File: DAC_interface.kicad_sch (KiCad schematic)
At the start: 2 parts

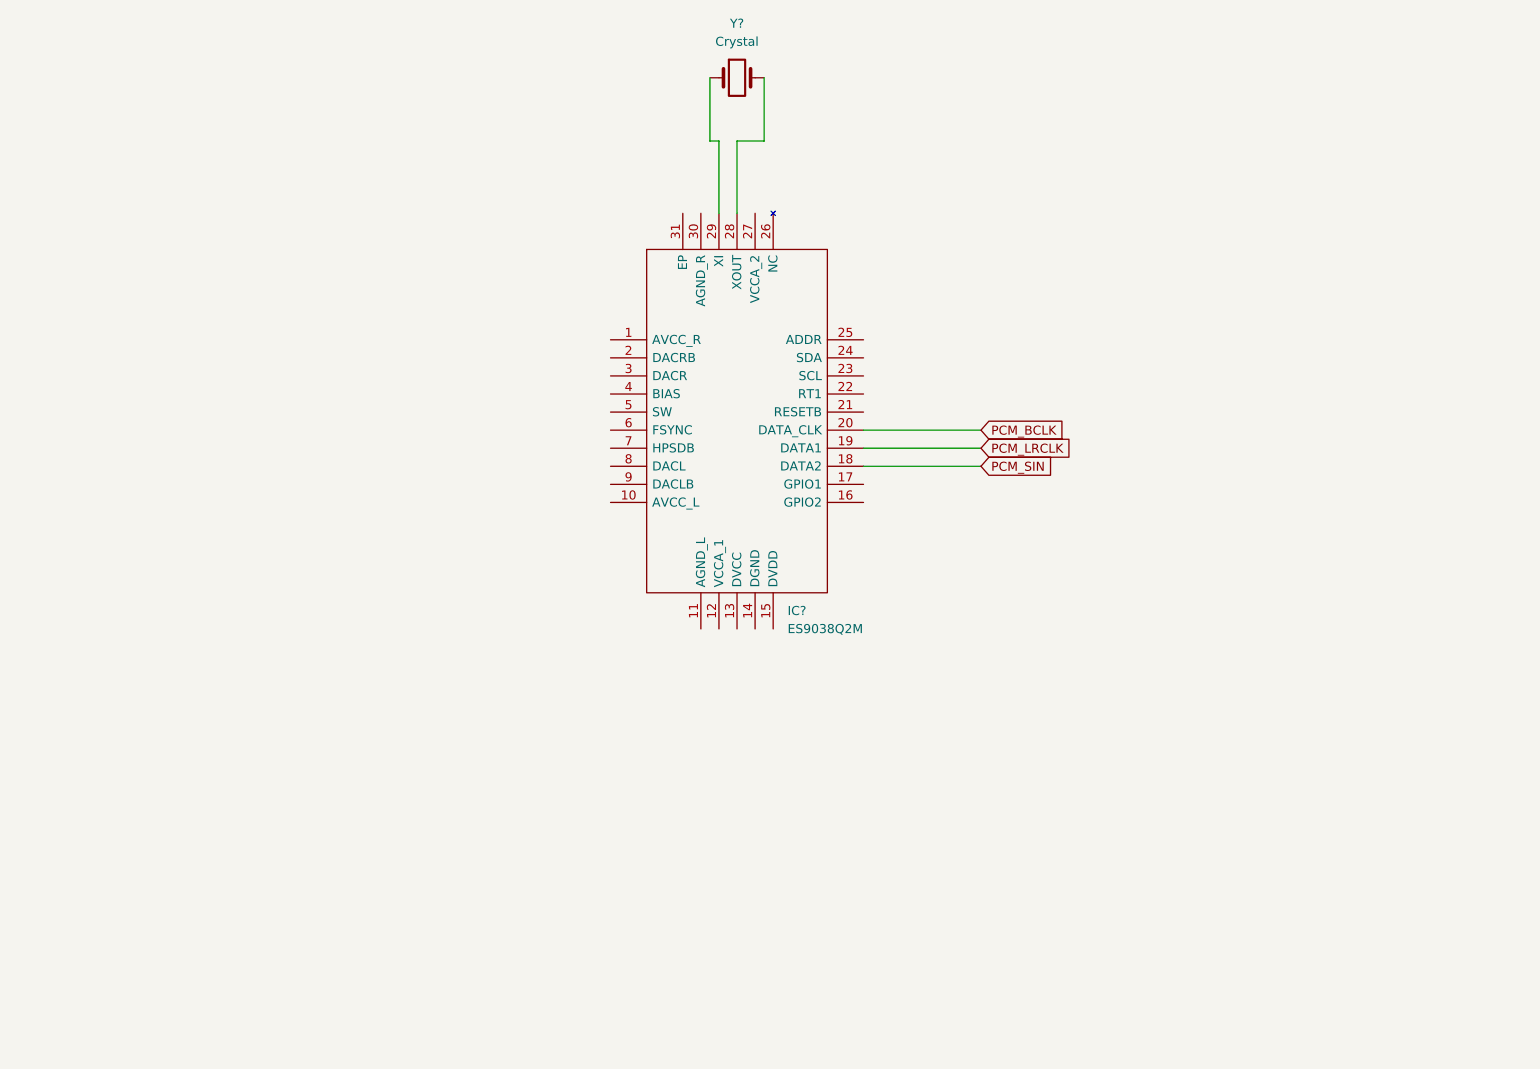
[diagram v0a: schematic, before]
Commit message: Adding ES9038q2m configuration
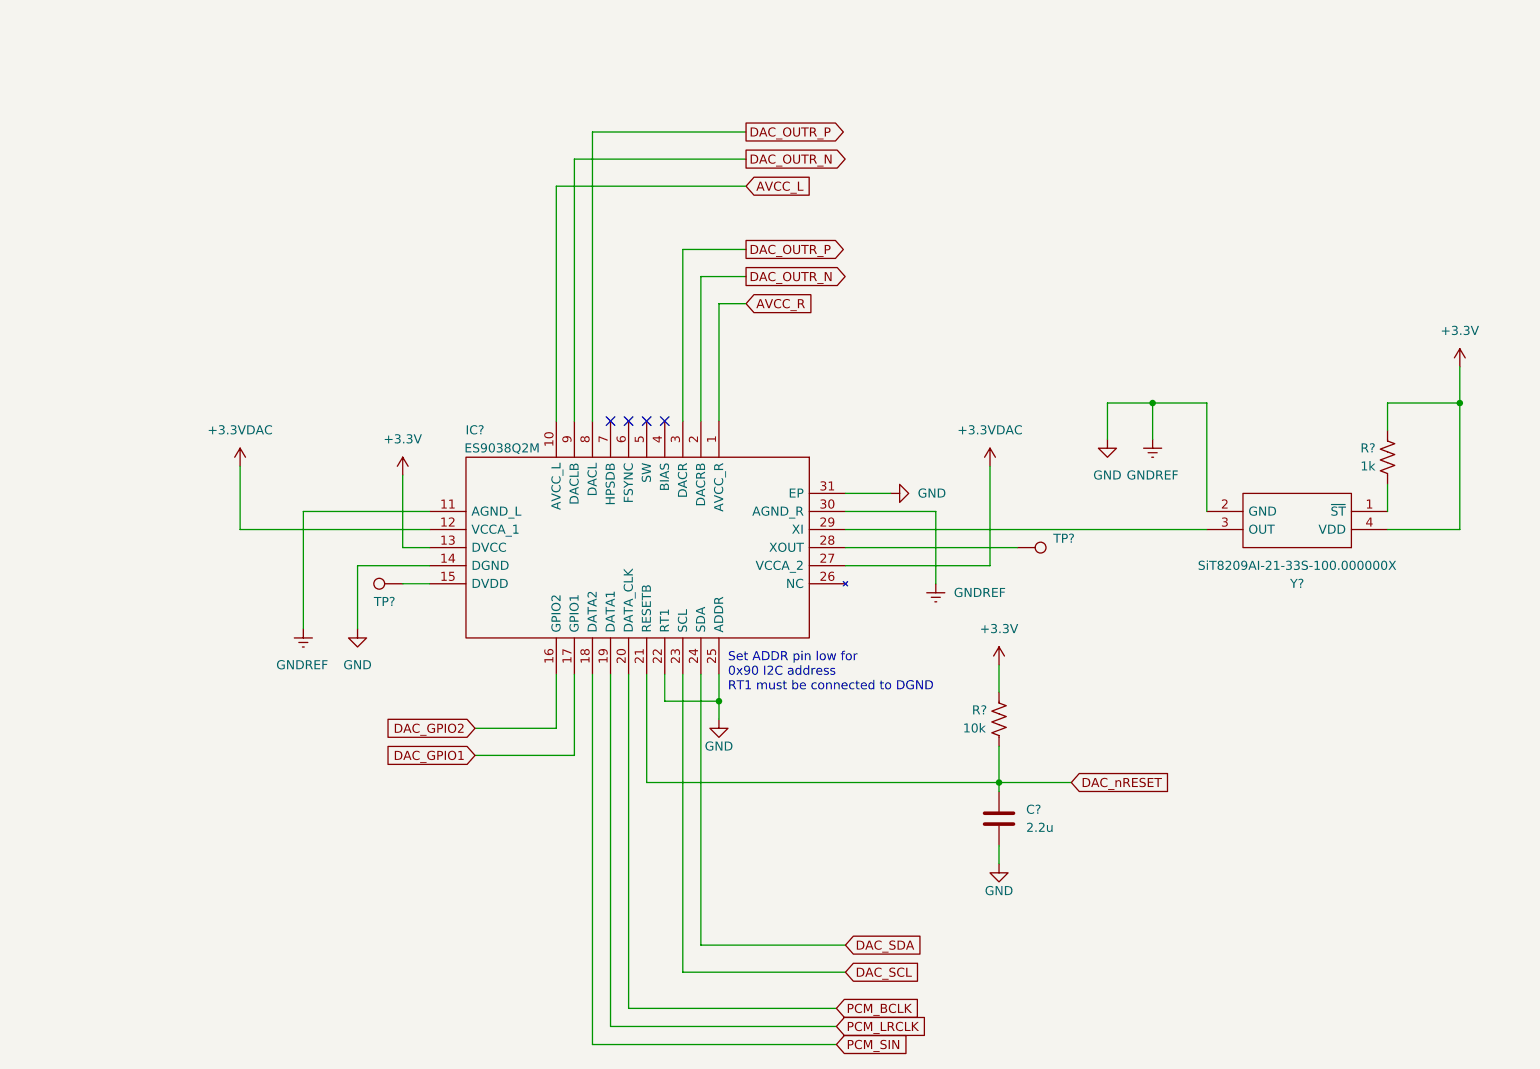
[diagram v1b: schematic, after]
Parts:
- removed Y?: Crystal, symbol Device:Crystal
- added C?: 2.2u, symbol Device:C
- added R?: 10k, symbol Device:R_US
- added R?: 1k, symbol Device:R_US
- added TP? (x2): TestPoint, symbol Connector:TestPoint
- added Y?: SiT8209AI-21-33S-100.000000X, SiT8209AI2133S100000000X, symbol SamacSys_Parts:SiT8209AI-21-33S-100.000000X
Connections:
- net at IC?.29 (XI): now also Y?.3 (OUT)
- net at IC?.28 (XOUT): now also TP?.1
- net AVCC_R: now reaches IC?.1 (AVCC_R)
- net AVCC_L: now reaches IC?.10 (AVCC_L)
- net GND: now reaches IC?.11 (AGND_L)
- net GND: now also IC?.14 (DGND), IC?.22 (RT1), IC?.25 (ADDR), IC?.30 (AGND_R), IC?.31 (EP), C?.2, Y?.2 (GND)
- net +3.3VDAC: now reaches IC?.12 (VCCA_1)
- net +3.3VDAC: now also IC?.27 (VCCA_2)
- net +3V3: now reaches IC?.13 (DVCC)
- net +3V3: now also R?.1, R?.1, Y?.4 (VDD)
- net at IC?.15 (DVDD): now also TP?.1
- net DAC_GPIO2: now reaches IC?.16 (GPIO2)
- net DAC_GPIO1: now reaches IC?.17 (GPIO1)
- net DAC_OUTR_N: now reaches IC?.2 (DACRB)
- net DAC_OUTR_N: now also IC?.9 (DACLB)
- net DAC_nRESET: now reaches IC?.21 (RESETB)
- net DAC_nRESET: now also C?.1, R?.2
- net DAC_SCL: now reaches IC?.23 (SCL)
- net DAC_SDA: now reaches IC?.24 (SDA)
- net DAC_OUTR_P: now reaches IC?.3 (DACR)
- net DAC_OUTR_P: now also IC?.8 (DACL)
- new net: R?.2, Y?.1 (~{ST})
- no-connect marks 0 -> 4
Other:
- note added: "Set ADDR pin low for 0x90 I2C address RT1 must be connected to DGND"
- title: (none) -> ES9038Q2M DAC Interface
- moved on the sheet: IC?

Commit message: WIP output stage
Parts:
- removed TP?: TestPoint, symbol Connector:TestPoint
- added C? (x2): 2.2u, symbol Device:C
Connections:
- net GND: now also C?.2, C?.2
- net at IC?.15 (DVDD): now also C?.1, C?.1
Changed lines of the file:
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@@
     (title "ES9038Q2M DAC Interface")
   )
+  (junction (at 60.96 113.03) (diameter 0) (color 0 0 0 0)
+  )
   (junction (at 182.88 140.97) (diameter 0) (color 0 0 0 0)
   )
@@
   )
   (junction (at 204.47 87.63) (diameter 0) (color 0 0 0 0)
+  )
+  (junction (at 57.15 120.65) (diameter 0) (color 0 0 0 0)
   )
   (junction (at 143.51 129.54) (diameter 0) (color 0 0 0 0)
@@
     (stroke (width 0) (type default) (color 0 0 0 0))
   )
+  (wire (pts (xy 53.34 120.65) (xy 57.15 120.65))
+    (stroke (width 0) (type default) (color 0 0 0 0))
+  )
   (wire (pts (xy 212.09 87.63) (xy 204.47 87.63))
     (stroke (width 0) (type default) (color 0 0 0 0))
@@
     (stroke (width 0) (type default) (color 0 0 0 0))
   )
+  (wire (pts (xy 53.34 113.03) (xy 60.96 113.03))
+    (stroke (width 0) (type default) (color 0 0 0 0))
+  )
   (wire (pts (xy 140.97 163.83) (xy 161.29 163.83))
     (stroke (width 0) (type default) (color 0 0 0 0))
@@
     (stroke (width 0) (type default) (color 0 0 0 0))
   )
+  (wire (pts (xy 57.15 124.46) (xy 57.15 120.65))
+    (stroke (width 0) (type default) (color 0 0 0 0))
+  )
   (wire (pts (xy 125.73 125.73) (xy 125.73 177.8))
     (stroke (width 0) (type default) (color 0 0 0 0))
@@
     (stroke (width 0) (type default) (color 0 0 0 0))
   )
-  (wire (pts (xy 99.06 113.03) (xy 102.87 113.03))
+  (wire (pts (xy 60.96 113.03) (xy 102.87 113.03))
     (stroke (width 0) (type default) (color 0 0 0 0))
   )
@@
   )
   (wire (pts (xy 161.29 105.41) (xy 212.09 105.41))
+    (stroke (width 0) (type default) (color 0 0 0 0))
+  )
+  (wire (pts (xy 57.15 120.65) (xy 60.96 120.65))
     (stroke (width 0) (type default) (color 0 0 0 0))
   )
@@
     )
   )
-  (global_label "DAC_GPIO1" (shape input) (at 109.22 137.16 180) (fields_autoplaced)
+  (global_label "DAC_GPIO1" (shape bidirectional) (at 109.22 137.16 180) (fields_autoplaced)
     (effects (font (size 1.27 1.27)) (justify right))
-    (property "Intersheet References" "${INTERSHEET_REFS}" (id 0) (at 96.5259 137.2394 0)
+    (property "Intersheet References" "${INTERSHEET_REFS}" (id 0) (at 96.5259 137.0806 0)
       (effects (font (size 1.27 1.27)) (justify right) hide)
     )
@@
     )
   )
-  (global_label "DAC_GPIO2" (shape input) (at 109.22 133.35 180) (fields_autoplaced)
+  (global_label "DAC_GPIO2" (shape bidirectional) (at 109.22 133.35 180) (fields_autoplaced)
     (effects (font (size 1.27 1.27)) (justify right))
-    (property "Intersheet References" "${INTERSHEET_REFS}" (id 0) (at 96.5259 133.4294 0)
+    (property "Intersheet References" "${INTERSHEET_REFS}" (id 0) (at 96.5259 133.2706 0)
       (effects (font (size 1.27 1.27)) (justify right) hide)
     )
@@
     (pin "2")
   )
+  (symbol (lib_id "power:GND") (at 57.15 124.46 0) (unit 1)
+    (in_bom yes) (on_board yes) (fields_autoplaced)
+    (property "Reference" "#PWR?" (id 0) (at 57.15 130.81 0)
+      (effects (font (size 1.27 1.27)) hide)
+    )
+    (property "Value" "GND" (id 1) (at 57.15 129.54 0))
+    (property "Footprint" "" (id 2) (at 57.15 124.46 0)
+      (effects (font (size 1.27 1.27)) hide)
+    )
+    (property "Datasheet" "" (id 3) (at 57.15 124.46 0)
+      (effects (font (size 1.27 1.27)) hide)
+    )
+    (pin "1")
+  )
   (symbol (lib_id "power:GND") (at 92.71 119.38 0) (unit 1)
     (in_bom yes) (on_board yes) (fields_autoplaced)
@@
     (pin "1")
   )
+  (symbol (lib_id "Device:C") (at 53.34 116.84 0) (unit 1)
+    (in_bom yes) (on_board yes)
+    (property "Reference" "C?" (id 0) (at 48.26 115.57 0)
+      (effects (font (size 1.27 1.27)) (justify left))
+    )
+    (property "Value" "2.2u" (id 1) (at 45.72 118.11 0)
+      (effects (font (size 1.27 1.27)) (justify left))
+    )
+    (property "Footprint" "" (id 2) (at 54.3052 120.65 0)
+      (effects (font (size 1.27 1.27)) hide)
+    )
+    (property "Datasheet" "~" (id 3) (at 53.34 116.84 0)
+      (effects (font (size 1.27 1.27)) hide)
+    )
+    (pin "1")
+    (pin "2")
+  )
   (symbol (lib_id "Connector:TestPoint") (at 185.42 107.95 270) (unit 1)
     (in_bom yes) (on_board yes) (fields_autoplaced)
@@
     (pin "1")
   )
-  (symbol (lib_id "Connector:TestPoint") (at 99.06 113.03 90) (unit 1)
-    (in_bom yes) (on_board yes)
-    (property "Reference" "TP?" (id 0) (at 96.52 115.57 90))
-    (property "Value" "TestPoint" (id 1) (at 93.98 111.7601 90)
-      (effects (font (size 1.27 1.27)) (justify left) hide)
-    )
-    (property "Footprint" "" (id 2) (at 99.06 107.95 0)
-      (effects (font (size 1.27 1.27)) hide)
-    )
-    (property "Datasheet" "~" (id 3) (at 99.06 107.95 0)
-      (effects (font (size 1.27 1.27)) hide)
-    )
-    (pin "1")
-  )
   (symbol (lib_id "power:+3.3VDAC") (at 181.61 96.52 0) (unit 1)
     (in_bom yes) (on_board yes) (fields_autoplaced)
@@
     (pin "1")
   )
+  (symbol (lib_id "Device:C") (at 60.96 116.84 0) (unit 1)
+    (in_bom yes) (on_board yes) (fields_autoplaced)
+    (property "Reference" "C?" (id 0) (at 64.77 115.5699 0)
+      (effects (font (size 1.27 1.27)) (justify left))
+    )
+    (property "Value" "2.2u" (id 1) (at 64.77 118.1099 0)
+      (effects (font (size 1.27 1.27)) (justify left))
+    )
+    (property "Footprint" "" (id 2) (at 61.9252 120.65 0)
+      (effects (font (size 1.27 1.27)) hide)
+    )
+    (property "Datasheet" "~" (id 3) (at 60.96 116.84 0)
+      (effects (font (size 1.27 1.27)) hide)
+    )
+    (pin "1")
+    (pin "2")
+  )
   (symbol (lib_id "SamacSys_Parts:ES9038Q2M") (at 143.51 90.17 270) (unit 1)

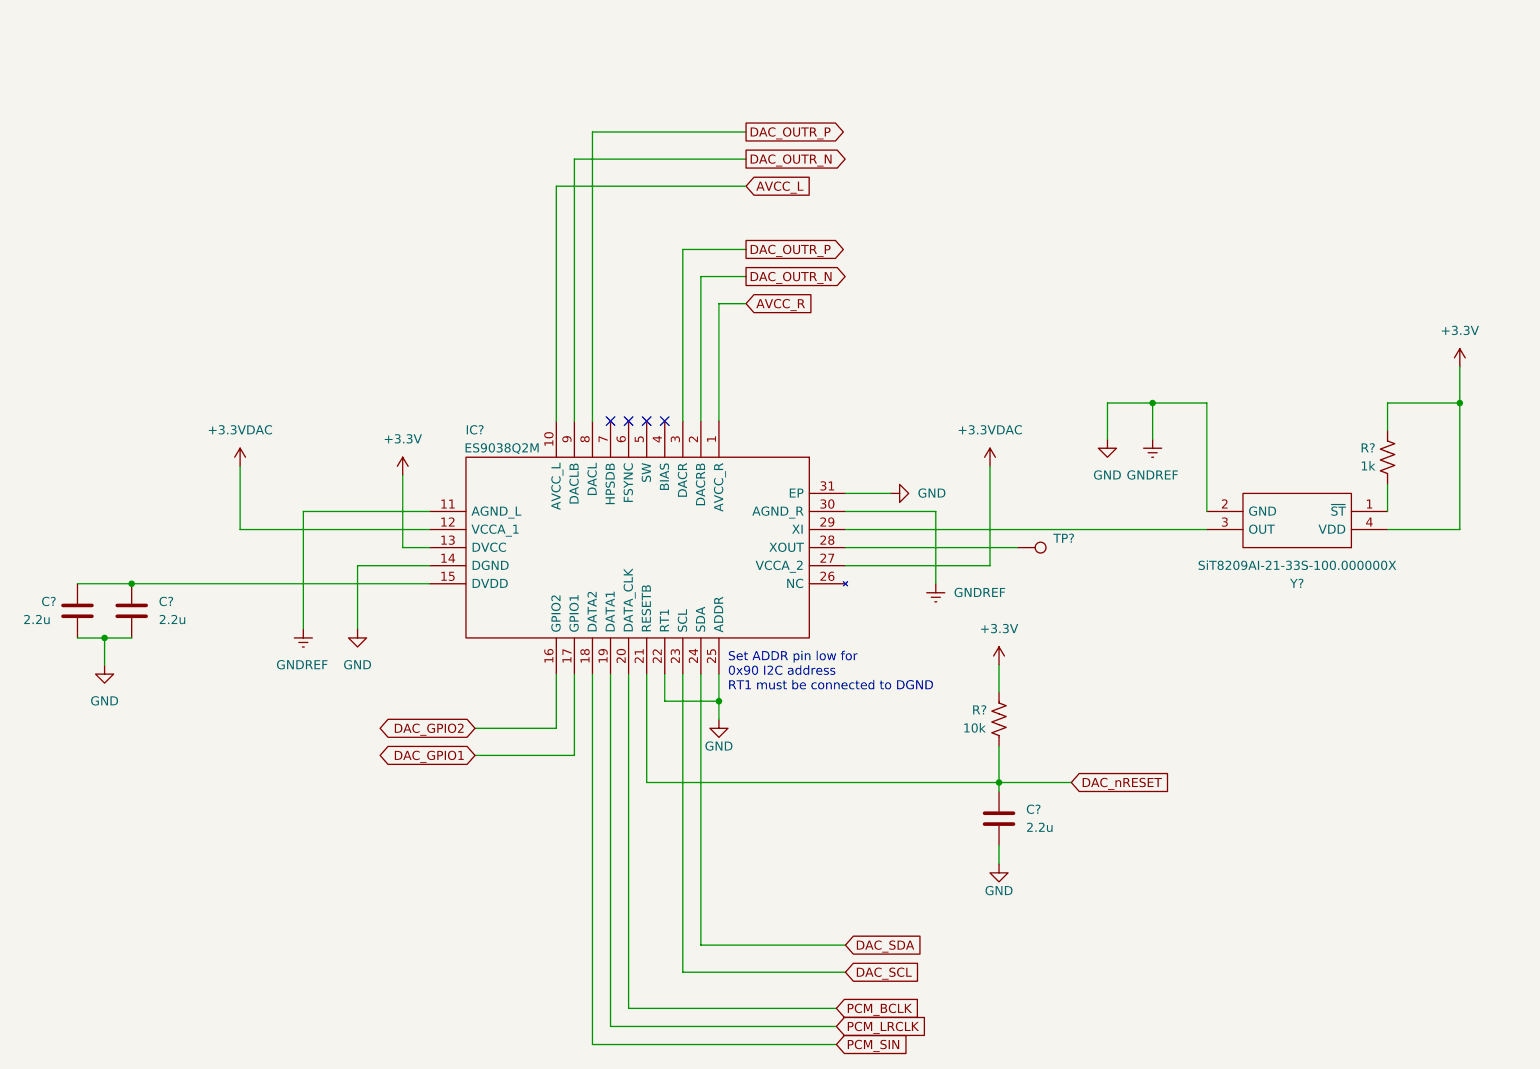
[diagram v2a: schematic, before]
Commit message: Adding values to output stage
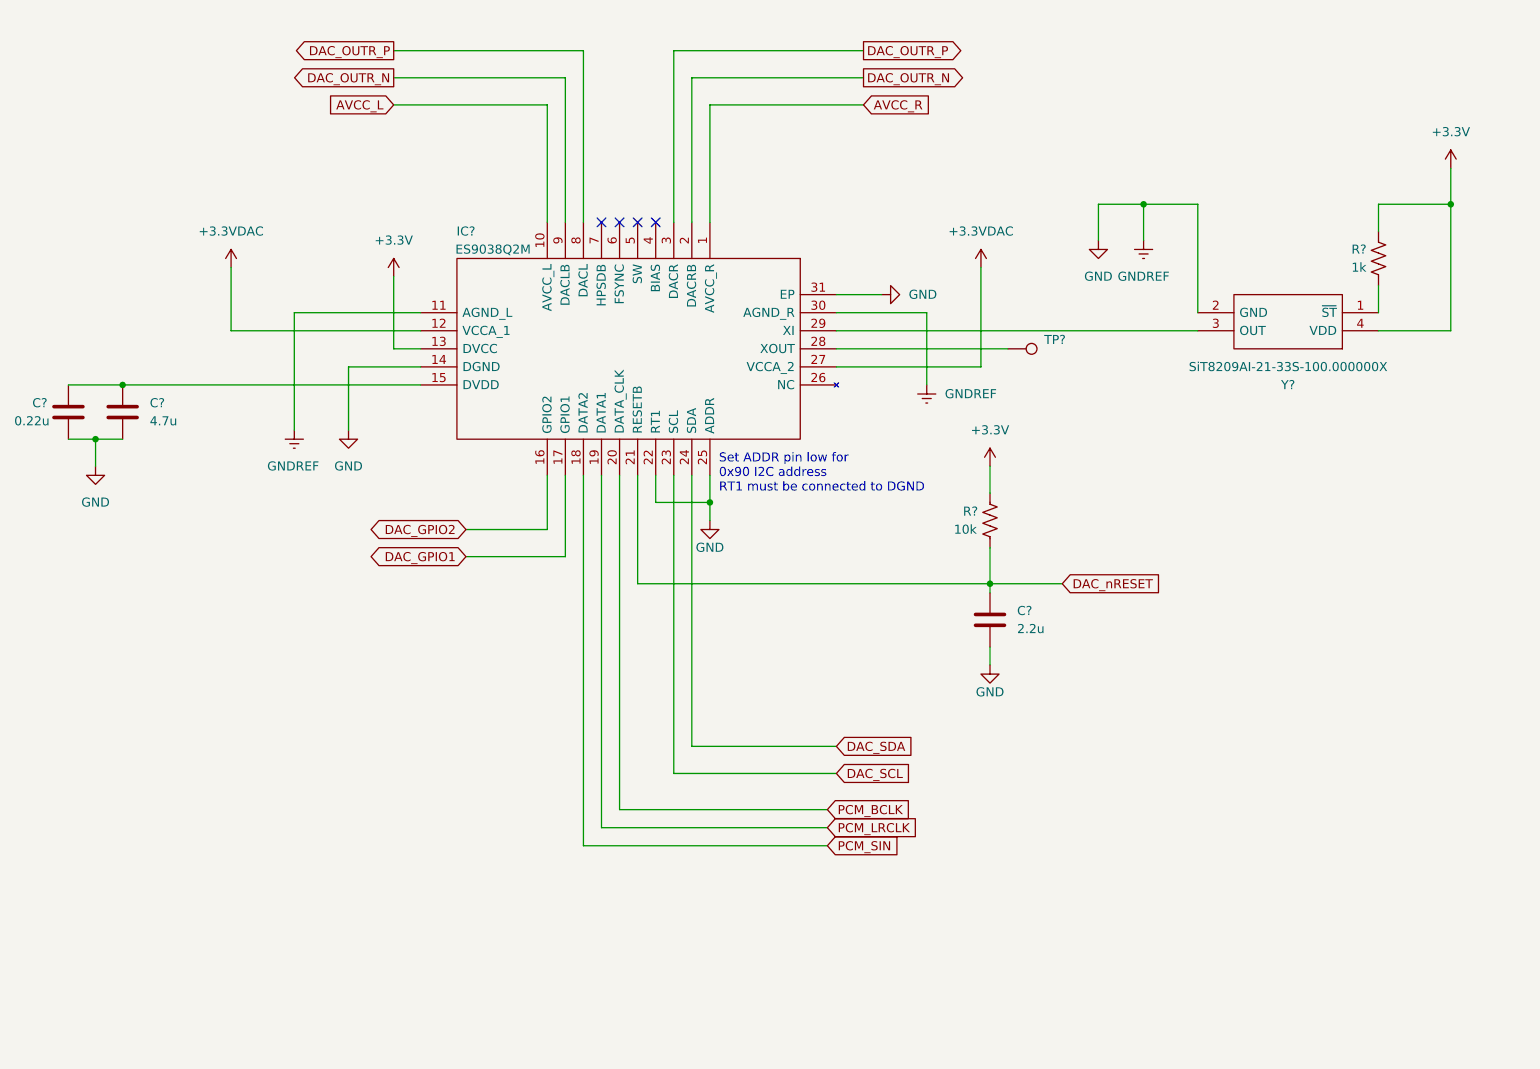
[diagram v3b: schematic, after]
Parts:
- C?: value 2.2u -> 0.22u
- C?: value 2.2u -> 4.7u
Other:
- moved on the sheet: C?, IC?, R?, TP?, Y?
